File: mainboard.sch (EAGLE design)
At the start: 34 parts, among them U1 ATMEGA2560AU, U10 MIC803-46D3VM3TR, U2 FT232RLSSOP, U3 RFM23BP, U4 HMC5883LSMD, U5 ITG-3200, U7 ATMEGA328P, U8 FT232RLSSOP, U9 MIC803-31D3VM3TR, Y1 RESONATORSMD, Y2 16MHZ

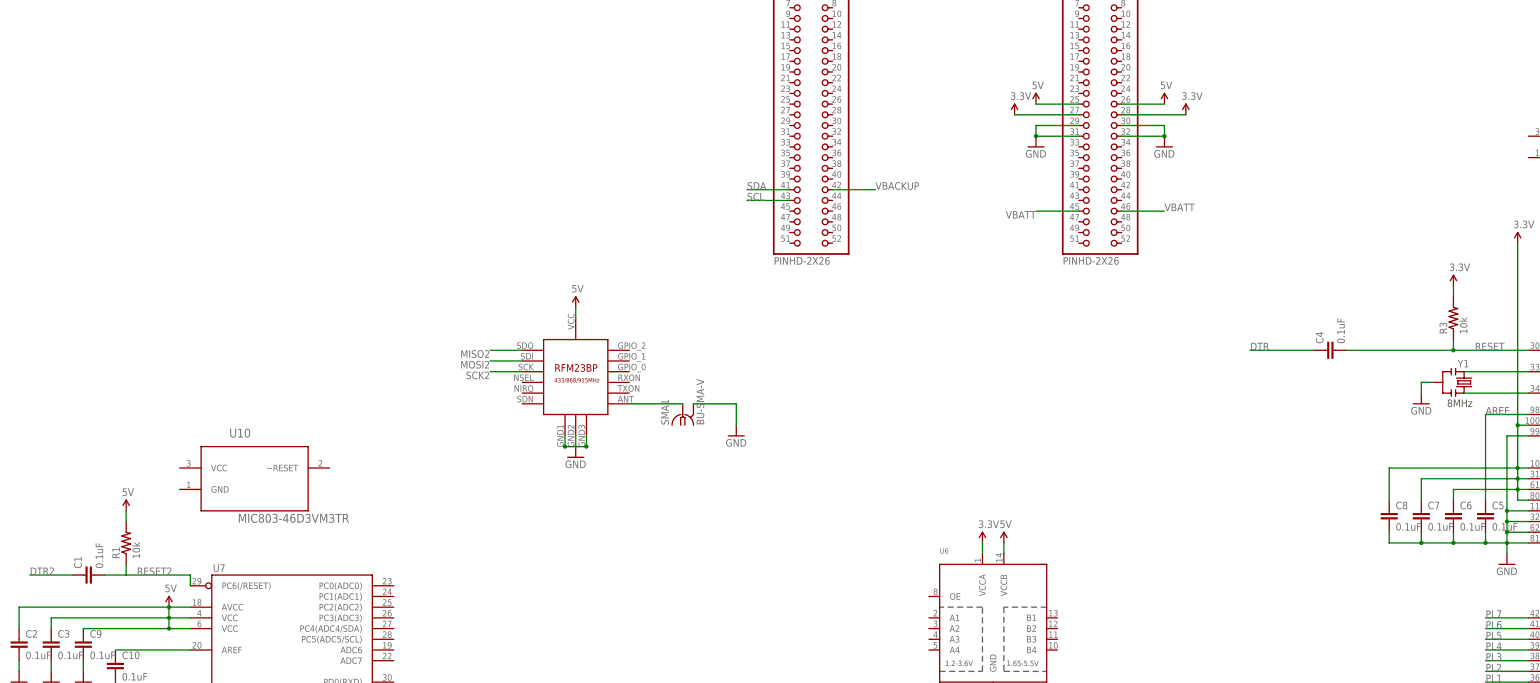
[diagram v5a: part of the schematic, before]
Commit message: Added new side solar panel
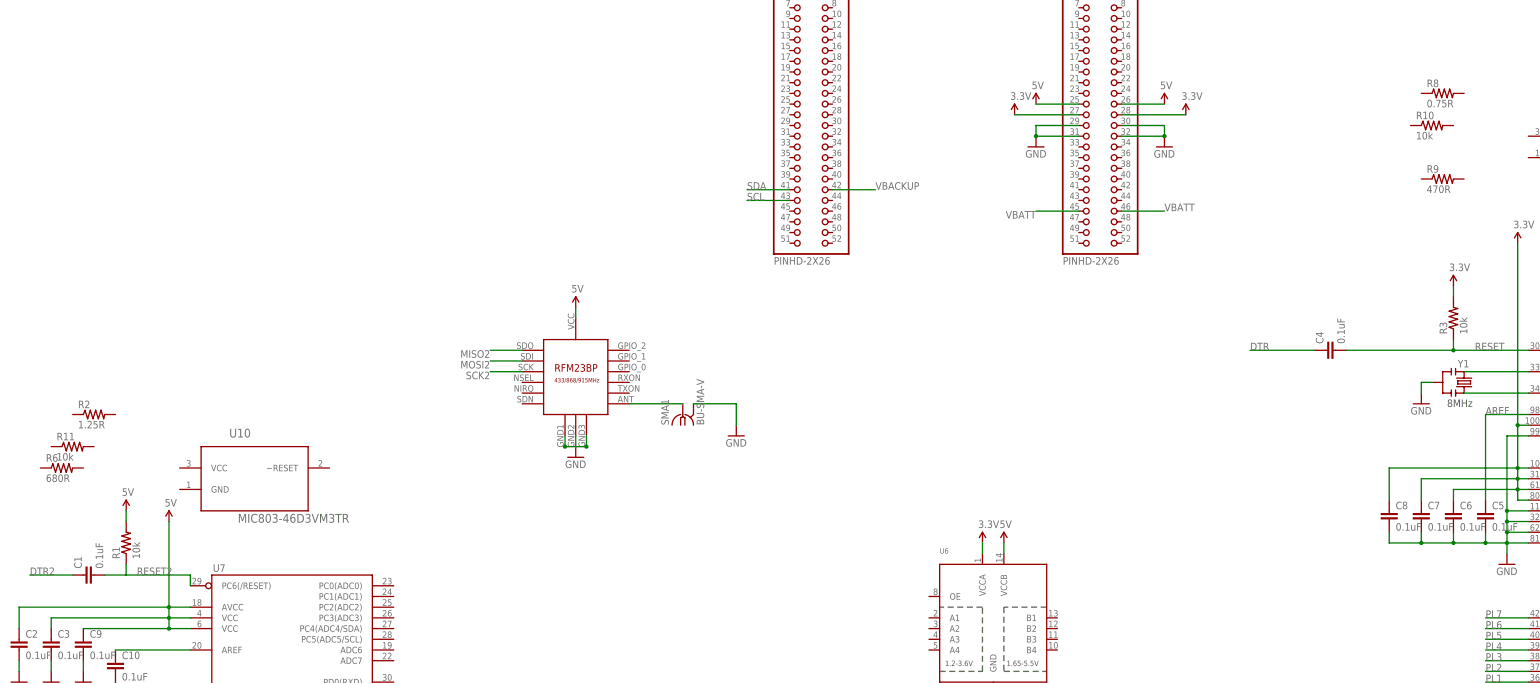
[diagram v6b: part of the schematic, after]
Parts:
- added R10, R11: 10k, SparkFun-Passives:RESISTOR0603-RES
- added R2: 1.25R, SparkFun-Passives:RESISTOR0603-RES
- added R6: 680R, SparkFun-Passives:RESISTOR0603-RES
- added R8: 0.75R, SparkFun-Passives:RESISTOR0603-RES
- added R9: 470R, SparkFun-Passives:RESISTOR0603-RES
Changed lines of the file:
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@@
 <part name="GND6" library="SparkFun" deviceset="GND" device=""/>
 <part name="GND7" library="SparkFun" deviceset="GND" device=""/>
-<part name="SUPPLY3" library="SparkFun-Aesthetics" deviceset="5V" device=""/>
 <part name="C10" library="SparkFun" deviceset="CAP" device="0603-CAP" value="0.1uF"/>
 <part name="GND8" library="SparkFun" deviceset="GND" device=""/>
@@
 <part name="U9" library="Micrel" deviceset="MIC803-31D3VM3TR" device=""/>
 <part name="U10" library="Micrel" deviceset="MIC803-46D3VM3TR" device=""/>
+<part name="R2" library="SparkFun-Passives" deviceset="RESISTOR" device="0603-RES" value="1.25R"/>
+<part name="R6" library="SparkFun-Passives" deviceset="RESISTOR" device="0603-RES" value="680R"/>
+<part name="R8" library="SparkFun-Passives" deviceset="RESISTOR" device="0603-RES" value="0.75R"/>
+<part name="R9" library="SparkFun-Passives" deviceset="RESISTOR" device="0603-RES" value="470R"/>
+<part name="R10" library="SparkFun-Passives" deviceset="RESISTOR" device="0603-RES" value="10k"/>
+<part name="R11" library="SparkFun-Passives" deviceset="RESISTOR" device="0603-RES" value="10k"/>
+<part name="SUPPLY7" library="SparkFun-Aesthetics" deviceset="5V" device=""/>
 </parts>
 <sheets>
@@
 <instance part="GND6" gate="1" x="-177.8" y="-20.32"/>
 <instance part="GND7" gate="1" x="-162.56" y="-20.32"/>
-<instance part="SUPPLY3" gate="G$1" x="-142.24" y="-2.54"/>
 <instance part="C10" gate="G$1" x="-154.94" y="-17.78"/>
 <instance part="GND8" gate="1" x="-154.94" y="-25.4"/>
@@
 <instance part="U9" gate="A" x="180.34" y="109.22"/>
 <instance part="U10" gate="A" x="-139.7" y="30.48"/>
+<instance part="R2" gate="G$1" x="-160.02" y="43.18"/>
+<instance part="R6" gate="G$1" x="-167.64" y="30.48"/>
+<instance part="R8" gate="G$1" x="160.02" y="119.38"/>
+<instance part="R9" gate="G$1" x="160.02" y="99.06"/>
+<instance part="R10" gate="G$1" x="157.48" y="111.76"/>
+<instance part="R11" gate="G$1" x="-165.1" y="35.56"/>
+<instance part="SUPPLY7" gate="G$1" x="-142.24" y="17.78"/>
 </instances>
 <busses>
@@
 </segment>
 <segment>
+<pinref part="U6" gate="G$1" pin="VCCB"/>
+<pinref part="SUPPLY4" gate="G$1" pin="5V"/>
+<wire x1="55.88" y1="10.16" x2="55.88" y2="12.7" width="0.1524" layer="91"/>
+</segment>
+<segment>
+<pinref part="H2" gate="G$1" pin="25"/>
+<wire x1="73.66" y1="116.84" x2="63.5" y2="116.84" width="0.1524" layer="91"/>
+<pinref part="SUPPLY5" gate="G$1" pin="5V"/>
+</segment>
+<segment>
+<pinref part="H2" gate="G$1" pin="26"/>
+<wire x1="83.82" y1="116.84" x2="93.98" y2="116.84" width="0.1524" layer="91"/>
+<pinref part="SUPPLY6" gate="G$1" pin="5V"/>
+</segment>
+<segment>
 <pinref part="U7" gate="G$1" pin="AVCC"/>
 <pinref part="C2" gate="G$1" pin="1"/>
@@
 <wire x1="-142.24" y1="-2.54" x2="-177.8" y2="-2.54" width="0.1524" layer="91"/>
 <wire x1="-177.8" y1="-2.54" x2="-177.8" y2="-7.62" width="0.1524" layer="91"/>
-<pinref part="SUPPLY3" gate="G$1" pin="5V"/>
 <junction x="-142.24" y="-2.54"/>
 <pinref part="U7" gate="G$1" pin="VCC@2"/>
@@
 <junction x="-142.24" y="-5.08"/>
 <junction x="-142.24" y="-7.62"/>
-</segment>
-<segment>
-<pinref part="U6" gate="G$1" pin="VCCB"/>
-<pinref part="SUPPLY4" gate="G$1" pin="5V"/>
-<wire x1="55.88" y1="10.16" x2="55.88" y2="12.7" width="0.1524" layer="91"/>
-</segment>
-<segment>
-<pinref part="H2" gate="G$1" pin="25"/>
-<wire x1="73.66" y1="116.84" x2="63.5" y2="116.84" width="0.1524" layer="91"/>
-<pinref part="SUPPLY5" gate="G$1" pin="5V"/>
-</segment>
-<segment>
-<pinref part="H2" gate="G$1" pin="26"/>
-<wire x1="83.82" y1="116.84" x2="93.98" y2="116.84" width="0.1524" layer="91"/>
-<pinref part="SUPPLY6" gate="G$1" pin="5V"/>
-</segment>
-</net>
+<wire x1="-142.24" y1="-2.54" x2="-142.24" y2="17.78" width="0.1524" layer="91"/>
+<pinref part="SUPPLY7" gate="G$1" pin="5V"/>
+</segment>
+</net>

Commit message: Added latch-up protection circuits to main board
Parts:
- added Q1, Q2, Q3, Q4: MOSFET-PCHANNEL, SparkFun-DiscreteSemi:MOSFET-PCHANNEL
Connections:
- new net N$10: Q4.S, R8.1, U9.VCC
- new net N$11: Q3.D, Q4.G, R9.2
- new net N$12: Q1.D, Q2.G, R6.2
- new net N$13: Q2.S, R2.1, U10.VCC
- new net N$6: C6.1, C7.1, C8.1, Q4.D, R3.2, U1.AVCC, U1.VCC, U1.VCC1, U1.VCC2, U1.VCC3
- new net N$7: C2.1, C3.1, C9.1, Q2.D, R1.2, U7.AVCC, U7.VCC@1, U7.VCC@2
- new net N$8: Q3.G, R10.1, U9.~RESET
- new net N$9: Q1.G, R11.1, U10.~RESET
- net 3.3V: now also Q3.S, R10.2, R8.2; no longer C6.1, C7.1, C8.1, R3.2, U1.AVCC, U1.VCC, U1.VCC1, U1.VCC2, U1.VCC3
- net 5V: now also Q1.S, R11.2, R2.2; no longer C2.1, C3.1, C9.1, R1.2, U7.AVCC, U7.VCC@1, U7.VCC@2
- net GND: now also R6.1, R9.1, U10.GND, U9.GND
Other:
- moved on the sheet: C1, R1, R10, R11, R2, R6, R8, R9, SMA1, U10, U9

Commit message: Added breakout for USB and charging
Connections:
- net MISO2 renamed N$16
- net MOSI2 renamed N$15
- net SCK2 renamed N$14
- new net RX_RF: U6.B1, U7.PD0(RXD)
- new net TX_RF: U6.B2, U7.PD1(TXD)
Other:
- moved on the sheet: SMA1, U2, U6, U8
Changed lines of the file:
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@@
 <instance part="H1" gate="G$1" x="10.16" y="116.84"/>
 <instance part="H2" gate="G$1" x="78.74" y="116.84"/>
-<instance part="U3" gate="G$1" x="-22.86" y="27.94"/>
+<instance part="U3" gate="G$1" x="-40.64" y="-38.1"/>
 <instance part="U5" gate="G$1" x="347.98" y="0"/>
 <instance part="U4" gate="G$1" x="355.6" y="-48.26"/>
-<instance part="U2" gate="G$1" x="-5.08" y="-60.96"/>
-<instance part="U6" gate="G$1" x="53.34" y="-7.62"/>
+<instance part="U2" gate="G$1" x="-106.68" y="-116.84"/>
+<instance part="U6" gate="G$1" x="53.34" y="-7.62" rot="MR0"/>
 <instance part="U1" gate="1" x="215.9" y="-17.78" smashed="yes">
 <attribute name="NAME" x="185.42" y="62.23" size="1.778" layer="95"/>
@@
 <instance part="C1" gate="G$1" x="-160.02" y="2.54" rot="R90"/>
 <instance part="R1" gate="G$1" x="-152.4" y="10.16" rot="R90"/>
-<instance part="SMA1" gate="G$1" x="2.54" y="20.32" rot="R90"/>
-<instance part="GND1" gate="1" x="15.24" y="15.24"/>
-<instance part="SUPPLY2" gate="G$1" x="-22.86" y="45.72"/>
-<instance part="GND3" gate="1" x="-22.86" y="10.16"/>
+<instance part="SMA1" gate="G$1" x="-15.24" y="-45.72" rot="R90"/>
+<instance part="GND1" gate="1" x="-2.54" y="-50.8"/>
+<instance part="SUPPLY2" gate="G$1" x="-40.64" y="-20.32"/>
+<instance part="GND3" gate="1" x="-40.64" y="-55.88"/>
 <instance part="C2" gate="G$1" x="-177.8" y="-12.7"/>
 <instance part="C3" gate="G$1" x="-170.18" y="-12.7"/>
@@
 <instance part="Y2" gate="G$1" x="-139.7" y="-25.4" rot="R270"/>
 <instance part="GND10" gate="1" x="-149.86" y="-35.56"/>
-<instance part="JP1" gate="G$1" x="60.96" y="-76.2"/>
-<instance part="U8" gate="G$1" x="30.48" y="-111.76"/>
-<instance part="JP2" gate="G$1" x="66.04" y="-119.38"/>
-<instance part="SUPPLY4" gate="G$1" x="55.88" y="12.7"/>
-<instance part="P+2" gate="G$1" x="50.8" y="12.7"/>
+<instance part="JP1" gate="G$1" x="175.26" y="-132.08"/>
+<instance part="U8" gate="G$1" x="220.98" y="-134.62"/>
+<instance part="JP2" gate="G$1" x="-55.88" y="-116.84"/>
+<instance part="SUPPLY4" gate="G$1" x="50.8" y="12.7"/>
+<instance part="P+2" gate="G$1" x="55.88" y="12.7"/>
 <instance part="GND11" gate="1" x="53.34" y="-27.94"/>
 <instance part="SUPPLY5" gate="G$1" x="63.5" y="116.84"/>
@@
 <segment>
 <pinref part="SMA1" gate="G$1" pin="2"/>
-<wire x1="5.08" y1="22.86" x2="15.24" y2="22.86" width="0.1524" layer="91"/>
-<wire x1="15.24" y1="22.86" x2="15.24" y2="17.78" width="0.1524" layer="91"/>
+<wire x1="-12.7" y1="-43.18" x2="-2.54" y2="-43.18" width="0.1524" layer="91"/>
+<wire x1="-2.54" y1="-43.18" x2="-2.54" y2="-48.26" width="0.1524" layer="91"/>
 <pinref part="GND1" gate="1" pin="GND"/>
 </segment>
@@
 <pinref part="U3" gate="G$1" pin="GND2"/>
 <pinref part="GND3" gate="1" pin="GND"/>
-<wire x1="-22.86" y1="15.24" x2="-22.86" y2="12.7" width="0.1524" layer="91"/>
+<wire x1="-40.64" y1="-50.8" x2="-40.64" y2="-53.34" width="0.1524" layer="91"/>
 <pinref part="U3" gate="G$1" pin="GND3"/>
-<wire x1="-20.32" y1="15.24" x2="-20.32" y2="12.7" width="0.1524" layer="91"/>
-<wire x1="-20.32" y1="12.7" x2="-22.86" y2="12.7" width="0.1524" layer="91"/>
+<wire x1="-38.1" y1="-50.8" x2="-38.1" y2="-53.34" width="0.1524" layer="91"/>
+<wire x1="-38.1" y1="-53.34" x2="-40.64" y2="-53.34" width="0.1524" layer="91"/>
 <pinref part="U3" gate="G$1" pin="GND1"/>
-<wire x1="-25.4" y1="15.24" x2="-25.4" y2="12.7" width="0.1524" layer="91"/>
-<wire x1="-22.86" y1="12.7" x2="-25.4" y2="12.7" width="0.1524" layer="91"/>
-<junction x="-25.4" y="12.7"/>
-<junction x="-20.32" y="12.7"/>
+<wire x1="-43.18" y1="-50.8" x2="-43.18" y2="-53.34" width="0.1524" layer="91"/>
+<wire x1="-40.64" y1="-53.34" x2="-43.18" y2="-53.34" width="0.1524" layer="91"/>
+<junction x="-43.18" y="-53.34"/>
+<junction x="-38.1" y="-53.34"/>
 </segment>
 <segment>
@@
 <pinref part="P+2" gate="G$1" pin="3.3V"/>
 <pinref part="U6" gate="G$1" pin="VCCA"/>
-<wire x1="50.8" y1="12.7" x2="50.8" y2="10.16" width="0.1524" layer="91"/>
+<wire x1="55.88" y1="12.7" x2="55.88" y2="10.16" width="0.1524" layer="91"/>
 </segment>
 <segment>
@@
 <pinref part="SUPPLY2" gate="G$1" pin="5V"/>
 <pinref part="U3" gate="G$1" pin="VCC"/>
-<wire x1="-22.86" y1="43.18" x2="-22.86" y2="45.72" width="0.1524" layer="91"/>
+<wire x1="-40.64" y1="-22.86" x2="-40.64" y2="-20.32" width="0.1524" layer="91"/>
 </segment>
 <segment>
 <pinref part="U6" gate="G$1" pin="VCCB"/>
 <pinref part="SUPPLY4" gate="G$1" pin="5V"/>
-<wire x1="55.88" y1="10.16" x2="55.88" y2="12.7" width="0.1524" layer="91"/>
+<wire x1="50.8" y1="10.16" x2="50.8" y2="12.7" width="0.1524" layer="91"/>
 </segment>
 <segment>
@@
 <pinref part="U3" gate="G$1" pin="ANT"/>
 <pinref part="SMA1" gate="G$1" pin="1"/>
-<wire x1="-10.16" y1="22.86" x2="2.54" y2="22.86" width="0.1524" layer="91"/>
+<wire x1="-27.94" y1="-43.18" x2="-15.24" y2="-43.18" width="0.1524" layer="91"/>
 </segment>
 </net>
@@
 <pinref part="Y2" gate="G$1" pin="3"/>
 <wire x1="-137.16" y1="-27.94" x2="-139.7" y2="-27.94" width="0.1524" layer="91"/>
-</segment>
-</net>
-<net name="MOSI2" class="0">
-<segment>
-<pinref part="U7" gate="G$1" pin="PB3(MOSI/OC2)"/>
-<wire x1="-88.9" y1="-50.8" x2="-78.74" y2="-50.8" width="0.1524" layer="91"/>
-<label x="-78.74" y="-50.8" size="1.778" layer="95"/>
-</segment>
-<segment>
-<pinref part="U3" gate="G$1" pin="SDI"/>
-<wire x1="-35.56" y1="33.02" x2="-43.18" y2="33.02" width="0.1524" layer="91"/>
-<label x="-43.18" y="33.02" size="1.778" layer="95" rot="R180"/>
-</segment>
-</net>
-<net name="MISO2" class="0">
-<segment>
-<pinref part="U7" gate="G$1" pin="PB4(MISO)"/>
-<wire x1="-88.9" y1="-53.34" x2="-78.74" y2="-53.34" width="0.1524" layer="91"/>
-<label x="-78.74" y="-53.34" size="1.778" layer="95"/>
-</segment>
-<segment>
-<pinref part="U3" gate="G$1" pin="SDO"/>
-<wire x1="-35.56" y1="35.56" x2="-43.18" y2="35.56" width="0.1524" layer="91"/>
-<label x="-43.18" y="35.56" size="1.778" layer="95" rot="R180"/>
-</segment>
-</net>
-<net name="SCK2" class="0">
-<segment>
-<pinref part="U7" gate="G$1" pin="PB5(SCK)"/>
-<wire x1="-88.9" y1="-55.88" x2="-78.74" y2="-55.88" width="0.1524" layer="91"/>
-<label x="-78.74" y="-55.88" size="1.778" layer="95"/>
-</segment>
-<segment>
-<pinref part="U3" gate="G$1" pin="SCK"/>
-<wire x1="-35.56" y1="30.48" x2="-43.18" y2="30.48" width="0.1524" layer="91"/>
-<label x="-43.18" y="30.48" size="1.778" layer="95" rot="R180"/>
 </segment>
 </net>
@@
 </segment>
 </net>
+<net name="RX_RF" class="0">
+<segment>
+<pinref part="U7" gate="G$1" pin="PD0(RXD)"/>
+<wire x1="-88.9" y1="-20.32" x2="-78.74" y2="-20.32" width="0.1524" layer="91"/>
+<label x="-78.74" y="-20.32" size="1.778" layer="95"/>
+</segment>
+<segment>
+<pinref part="U6" gate="G$1" pin="B1"/>
+<wire x1="38.1" y1="-5.08" x2="27.94" y2="-5.08" width="0.1524" layer="91"/>
+<label x="27.94" y="-5.08" size="1.778" layer="95"/>
+</segment>
+</net>
+<net name="TX_RF" class="0">
+<segment>
+<pinref part="U7" gate="G$1" pin="PD1(TXD)"/>
+<wire x1="-88.9" y1="-22.86" x2="-78.74" y2="-22.86" width="0.1524" layer="91"/>
+<label x="-78.74" y="-22.86" size="1.778" layer="95"/>
+</segment>
+<segment>
+<pinref part="U6" gate="G$1" pin="B2"/>
+<wire x1="38.1" y1="-7.62" x2="27.94" y2="-7.62" width="0.1524" layer="91"/>
+<label x="27.94" y="-7.62" size="1.778" layer="95"/>
+</segment>
+</net>
+<net name="N$14" class="0">
+<segment>
+<pinref part="U7" gate="G$1" pin="PB5(SCK)"/>
+<wire x1="-88.9" y1="-55.88" x2="-58.42" y2="-55.88" width="0.1524" layer="91"/>
+<wire x1="-58.42" y1="-55.88" x2="-58.42" y2="-35.56" width="0.1524" layer="91"/>
+<pinref part="U3" gate="G$1" pin="SCK"/>
+<wire x1="-58.42" y1="-35.56" x2="-53.34" y2="-35.56" width="0.1524" layer="91"/>
+</segment>
+</net>
+<net name="N$15" class="0">
+<segment>
+<pinref part="U7" gate="G$1" pin="PB3(MOSI/OC2)"/>
+<wire x1="-88.9" y1="-50.8" x2="-60.96" y2="-50.8" width="0.1524" layer="91"/>
+<wire x1="-60.96" y1="-50.8" x2="-60.96" y2="-33.02" width="0.1524" layer="91"/>
+<pinref part="U3" gate="G$1" pin="SDI"/>
+<wire x1="-60.96" y1="-33.02" x2="-53.34" y2="-33.02" width="0.1524" layer="91"/>
+</segment>
+</net>
+<net name="N$16" class="0">
+<segment>
+<pinref part="U7" gate="G$1" pin="PB4(MISO)"/>
+<wire x1="-88.9" y1="-53.34" x2="-63.5" y2="-53.34" width="0.1524" layer="91"/>
+<wire x1="-63.5" y1="-53.34" x2="-63.5" y2="-30.48" width="0.1524" layer="91"/>
+<pinref part="U3" gate="G$1" pin="SDO"/>
+<wire x1="-63.5" y1="-30.48" x2="-53.34" y2="-30.48" width="0.1524" layer="91"/>
+</segment>
+</net>
